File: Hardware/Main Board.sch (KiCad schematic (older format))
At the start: 20 parts, among them U1 SN75176BDR, U1 STM32F401RCT6, X1 24MHz

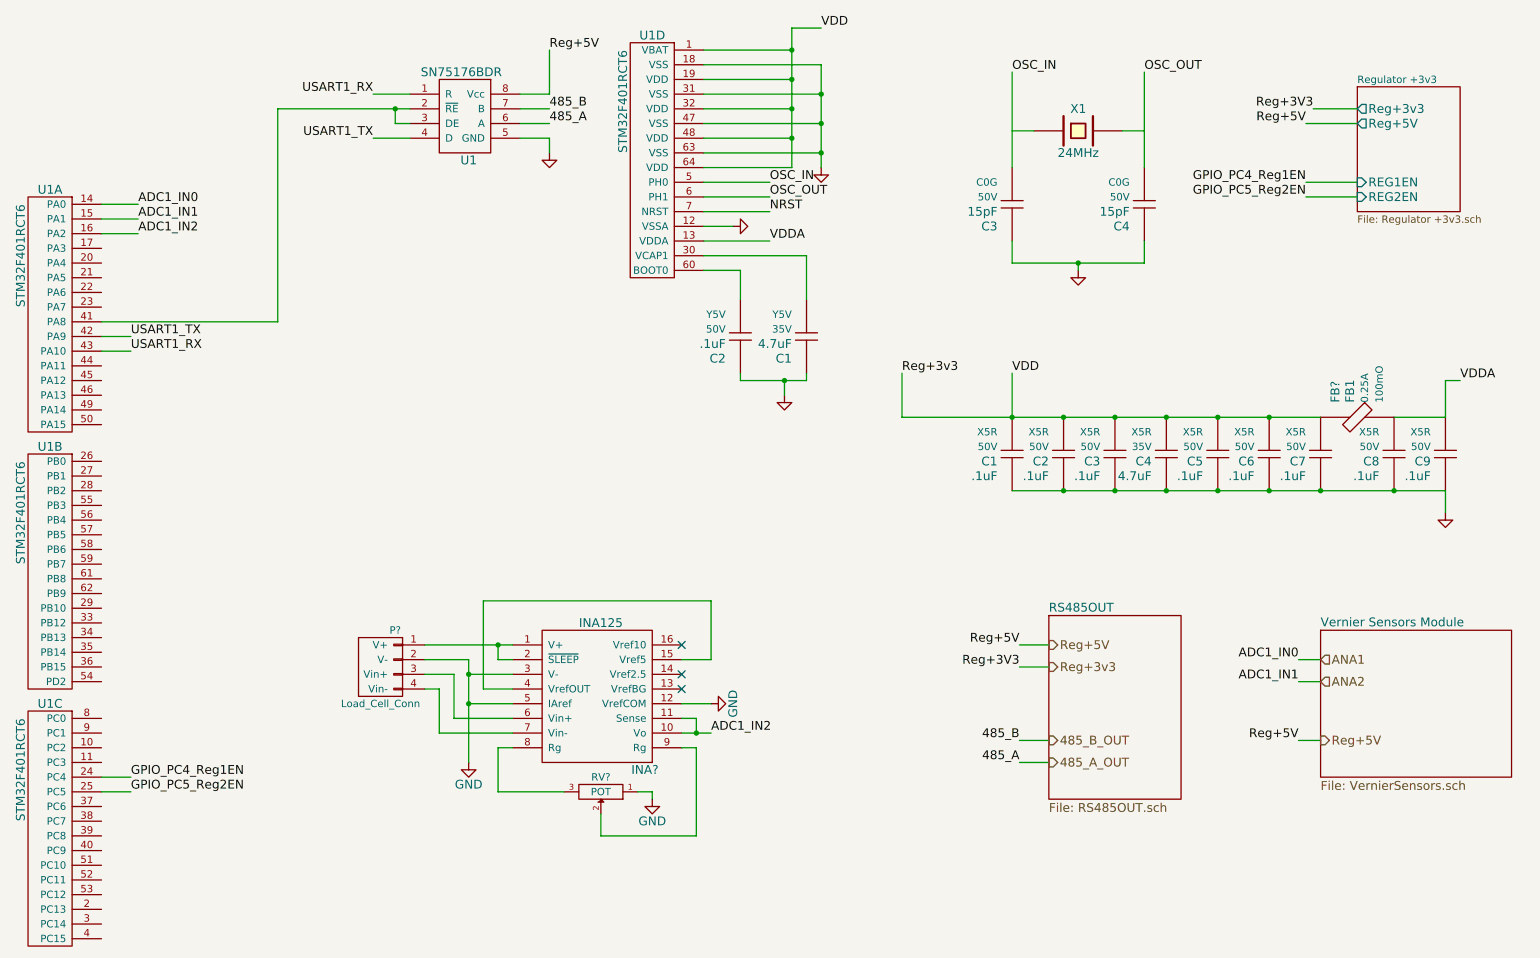
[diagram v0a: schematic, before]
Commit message: Add GPS Pads, potentiometer to INA125, 3v3 regulator always enabled, footprints created for GPS Pads and BTA, parts assigned
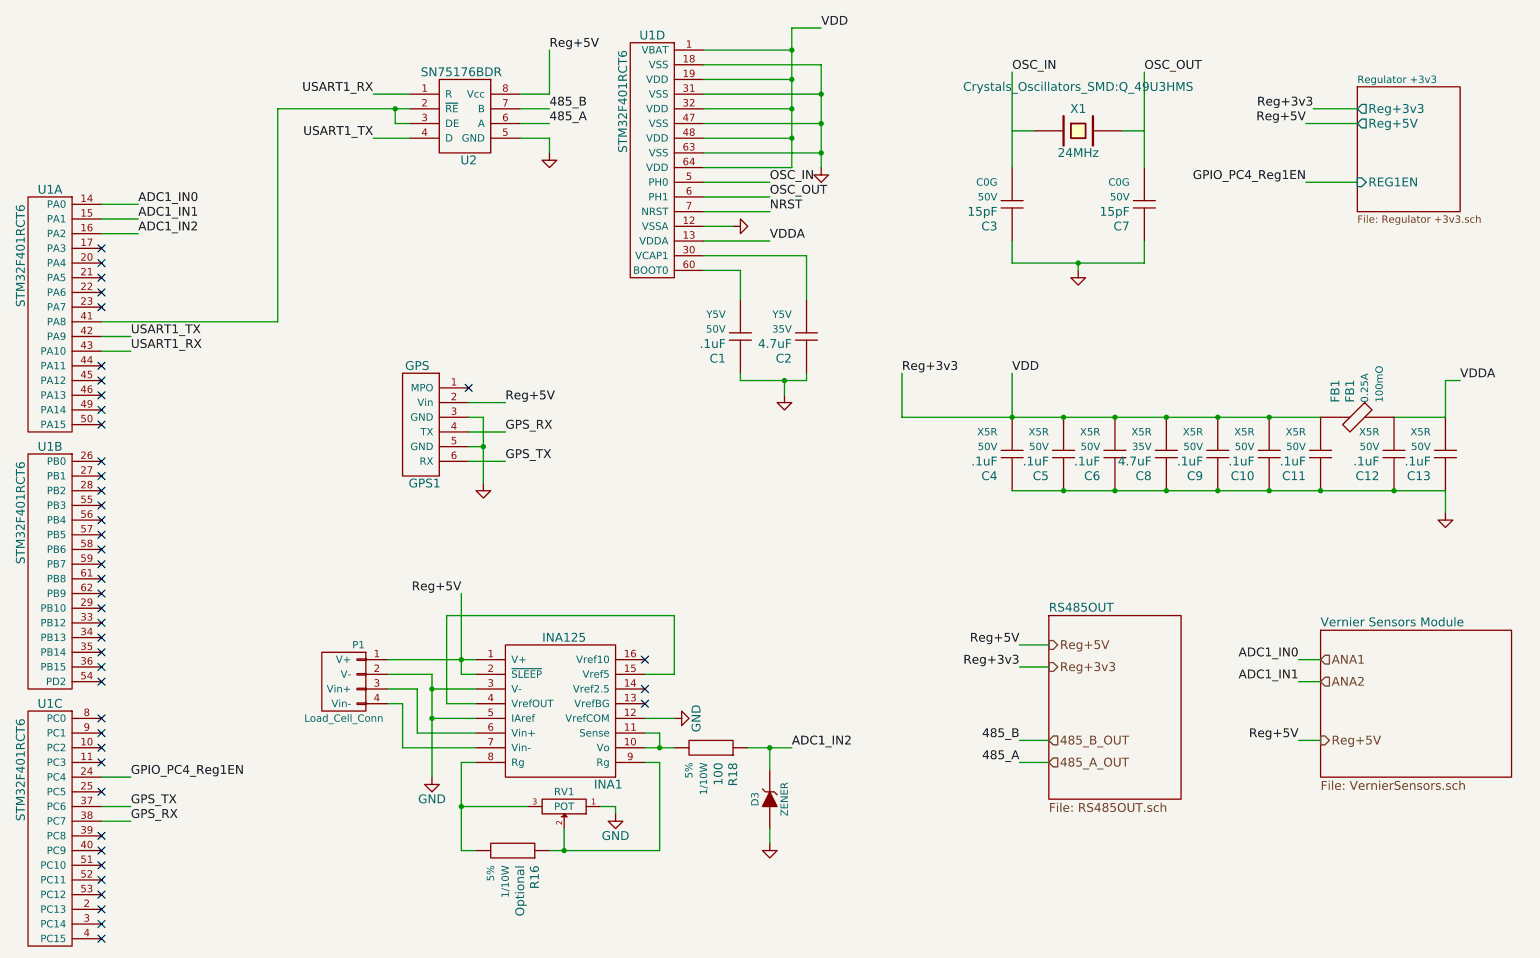
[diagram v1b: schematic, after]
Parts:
- added D3: ZENER, MAVRIc:Diode_MicroSMP, symbol ZENER
- added GPS1: GPS, MAVRIc:GPS_Pads, symbol GPS
- added R16: Optional, Resistors_SMD:R_1206_HandSoldering, symbol Resistor
- added R18: 100, Resistors_SMD:R_1206_HandSoldering, symbol Resistor
- C1: renamed from C2; footprint (none) -> Capacitors_SMD:C_1206_HandSoldering
- C10: renamed from .1uF; value C6 -> .1uF; footprint (none) -> Capacitors_SMD:C_1206_HandSoldering
- C11: renamed from .1uF; value C7 -> .1uF; footprint (none) -> Capacitors_SMD:C_1206_HandSoldering
- C12: renamed from .1uF; value C8 -> .1uF; footprint (none) -> Capacitors_SMD:C_1206_HandSoldering
- C13: renamed from .1uF; value C9 -> .1uF; footprint (none) -> Capacitors_SMD:C_1206_HandSoldering
- C2: renamed from C1; footprint (none) -> Capacitors_SMD:C_1206_HandSoldering
- C3: footprint (none) -> Capacitors_SMD:C_1206_HandSoldering
- C4: renamed from .1uF; value C1 -> .1uF; footprint (none) -> Capacitors_SMD:C_1206_HandSoldering
- C5: renamed from .1uF; value C2 -> .1uF; footprint (none) -> Capacitors_SMD:C_1206_HandSoldering
- C6: renamed from .1uF; value C3 -> .1uF; footprint (none) -> Capacitors_SMD:C_1206_HandSoldering
- C7: renamed from C4; footprint (none) -> Capacitors_SMD:C_1206_HandSoldering
- C8: renamed from 4.7uF; value C4 -> 4.7uF; footprint (none) -> Capacitors_SMD:C_1206_HandSoldering
- C9: renamed from .1uF; value C5 -> .1uF; footprint (none) -> Capacitors_SMD:C_1206_HandSoldering
- FB1: renamed from FB?; footprint (none) -> Resistors_SMD:R_1206_HandSoldering
- INA1: renamed from INA?; footprint (none) -> SMD_Packages:SO-16-N
- P1: renamed from P?; footprint (none) -> MAVRIc:1x4_Breakaway_Header
- RV1: renamed from RV?; footprint (none) -> Potentiometers:Potentiometer_Bourns_3005_Angular_ScrewFront
- U1: footprint (none) -> Housings_QFP:TQFP-64_10x10mm_Pitch0.5mm
- U2: renamed from U1; footprint (none) -> Housings_SOIC:SOIC-8_3.9x4.9mm_Pitch1.27mm
- X1: footprint ~ -> Crystals_Oscillators_SMD:Q_49U3HMS
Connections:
- net ADC1_IN2: now also D3.2 (K), R18.1; no longer INA1.10 (Vo), INA1.11 (Sense)
- net GND: now also D3.1 (A), GPS1.3 (GND), GPS1.5 (GND)
- net Reg+5V: now also INA1.1 (V+), INA1.2 (~SLEEP), P1.1 (V+), GPS1.2 (Vin)
- net GPS_TX: now reaches U1.37 (PC6)
- net GPS_TX: now also GPS1.6 (RX)
- net GPS_RX: now reaches U1.38 (PC7)
- net GPS_RX: now also GPS1.4 (TX)
- net at INA1.8 (Rg), RV1.3: now also R16.2
- net at INA1.9 (Rg), RV1.2: now also R16.1
- net GPIO_PC5_Reg2EN: no longer names the net of U1.25 (PC5)
- new net: INA1.10 (Vo), INA1.11 (Sense), R18.2
- no-connect marks 3 -> 43
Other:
- moved on the sheet: INA1, P1, RV1
